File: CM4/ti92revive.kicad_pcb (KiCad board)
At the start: 2 copper layers, 205 x 116.7 mm, 219 parts, among them J1 USB_B, J2 Conn_01x02, J3 Conn_01x02, Q1 EMH3, U1 Compute_Module_4_Connectors, U3 BQ25887RGET, U4 MAX17643, U5 ATTINY85-20PU, U6 TQ2SA-L2-3V-Z-Remake

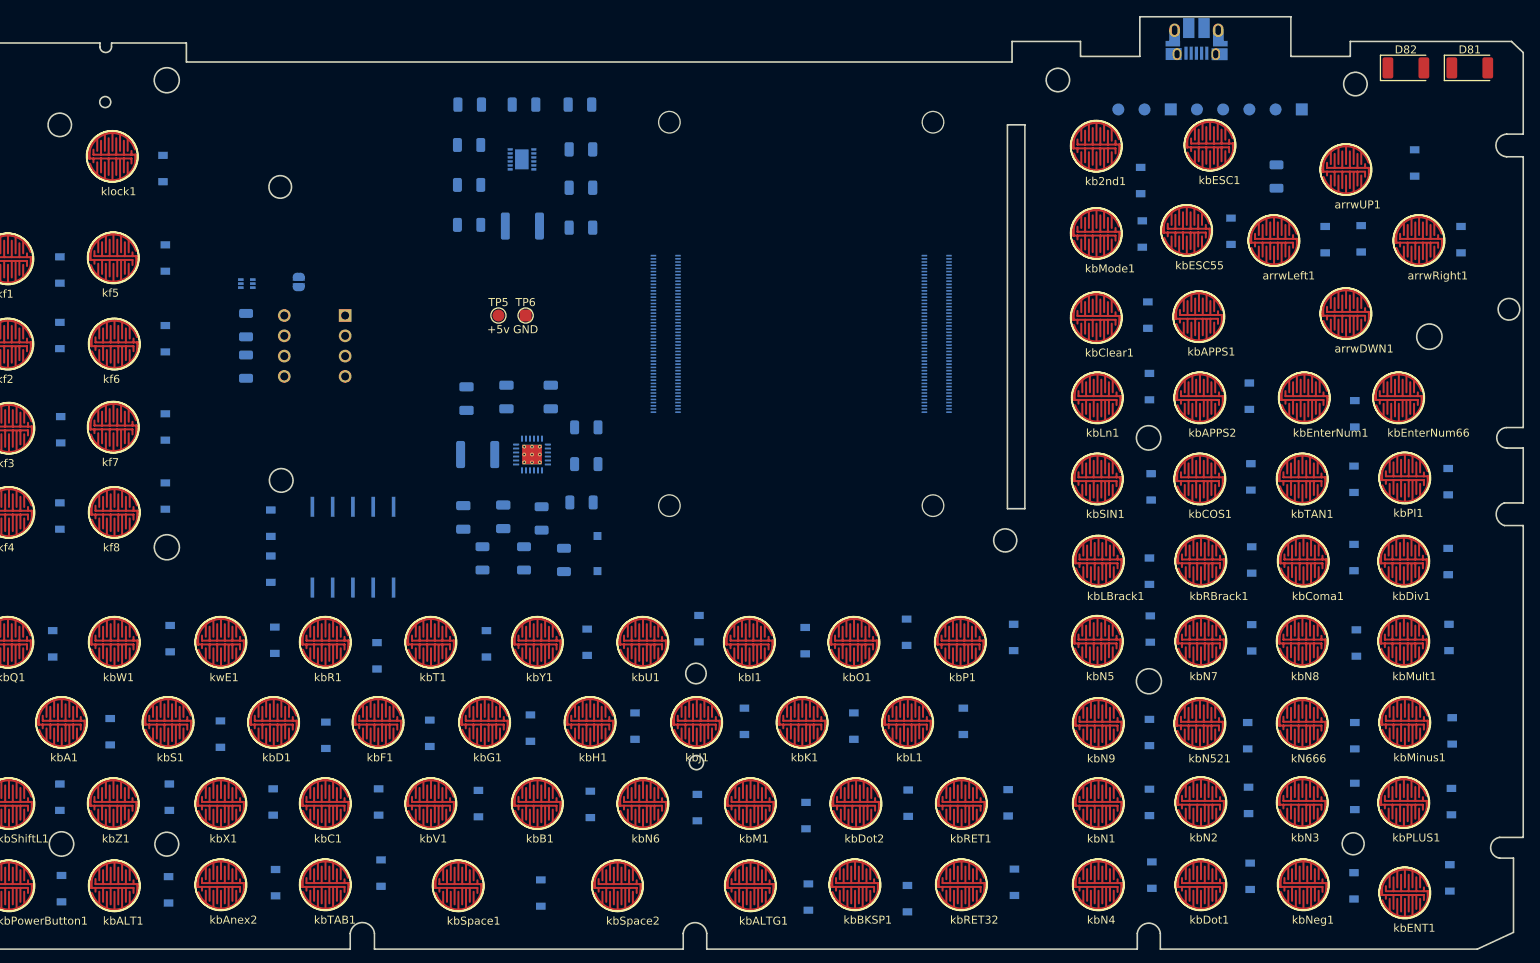
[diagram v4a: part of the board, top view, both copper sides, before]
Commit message: Removed Keyboard Matrix Diodes and Added PowerLED and ActivityLED
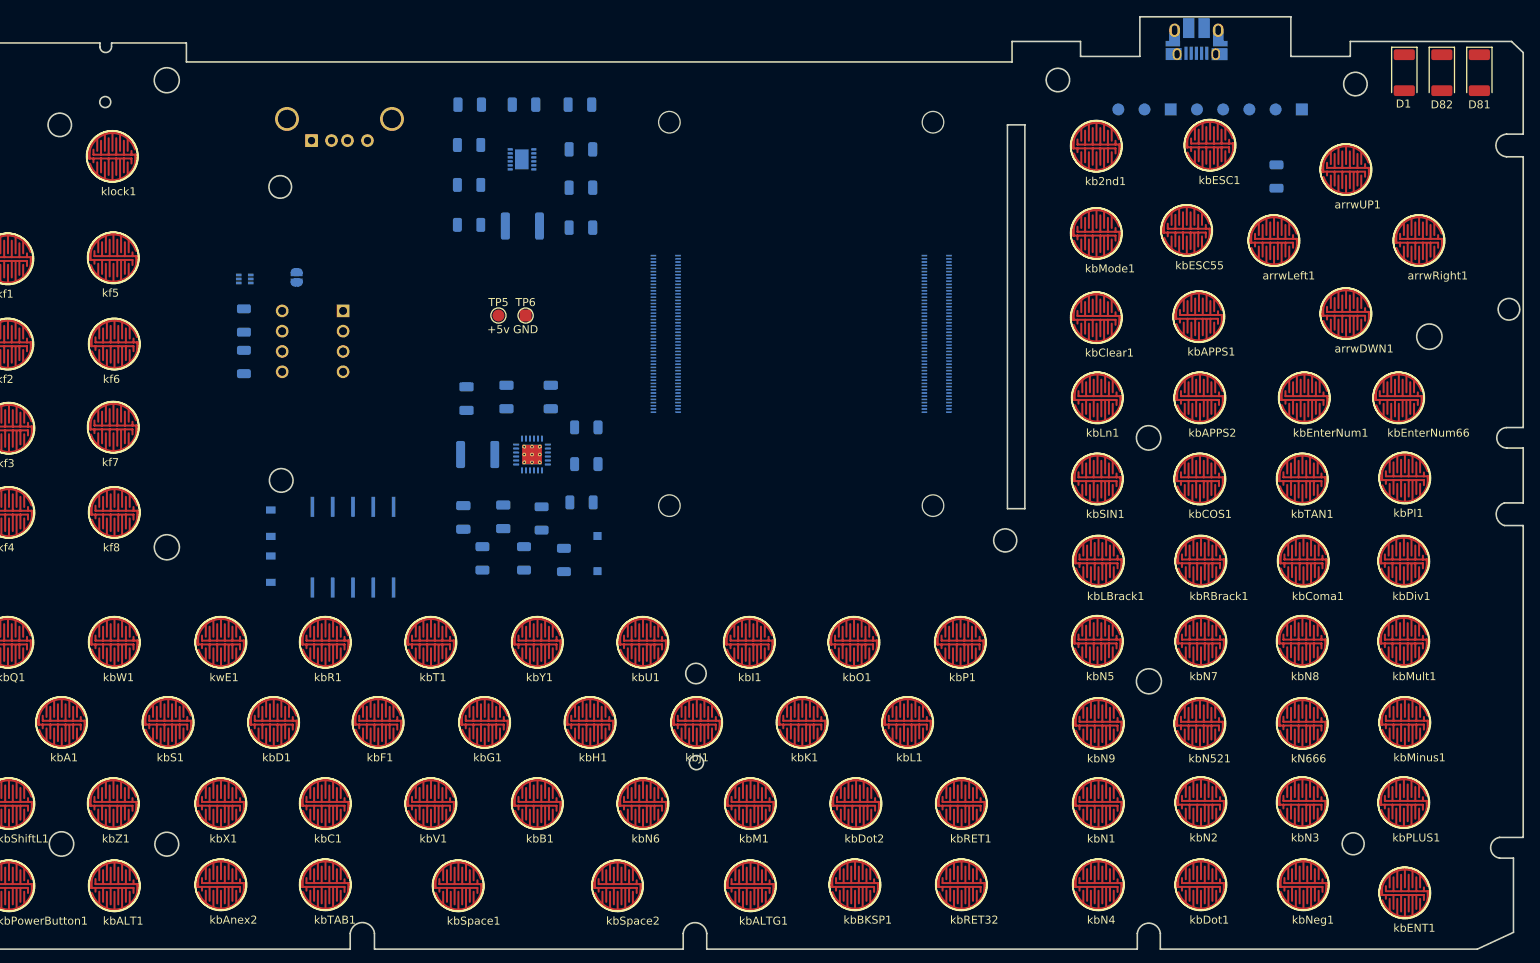
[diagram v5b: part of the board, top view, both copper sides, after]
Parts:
- removed D0, D10, D11, D12, D13, D14, D15, D16, D17, D18, D19, D2, D20, D21, D22, D23, D24, D25, D26, D27, D28, D29, D3, D30, D31, D32, D33, D34, D35, D36, D37, D38, D39, D4, D40, D41, D42, D43, D44, D45, D46, D47, D48, D49, D5, D50, D51, D52, D53, D54, D55, D56, D57, D58, D59, D6, D60, D61, D62, D63, D64, D65, D66, D67, D68, D69, D7, D70, D71, D72, D73, D74, D75, D76, D77, D78, D79, D8, D80, D9: 1N4148W, Diode_SMD:D_SOD-123
- added J4: USB_A, Connector_USB:USB_A_Stewart_SS-52100-001_Horizontal, B.Cu at (106.0, 47.9)
- D1: value 1N4148W -> Activity; footprint Diode_SMD:D_SOD-123 -> LED_SMD:LED_2010_5025Metric; moved to F.Cu
- JP1: value SolderJumper_2_Open -> PowerControllerBipass
- R12: value 330 -> 1K
- moved D1 170.1 mm to (242.8, 39.4), turned to -90 degrees
- moved D82 4.54 mm to (247.5, 39.4), turned to -90 degrees
- moved D81 1.34 mm to (252.2, 39.4), turned to -90 degrees
- moved JP1 0.64 mm to (104.1, 65.0)
- moved Q1 0.64 mm to (97.6, 65.2)
- moved R12 0.64 mm to (97.5, 70.4)
- moved R13 0.64 mm to (97.5, 75.6)
- moved U5 0.64 mm to (110.0, 69.2)
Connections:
- D1 pad 1: row0 -> +3.3
- R12 pad 1: unconnected-(R12-Pad1) -> Net-(D1-Pad2)
- R12 pad 2: Net-(R12-Pad2) -> Net-(U1-Pad21)
- U1 pad 101: unconnected-(U1-Pad101) -> Net-(U1-Pad101)
- U1 pad 103: unconnected-(U1-Pad103) -> Net-(U1-Pad103)
- U1 pad 105: unconnected-(U1-Pad105) -> Net-(U1-Pad105)
- U1 pad 21: unconnected-(U1-Pad21) -> Net-(U1-Pad21)
- U1 pad 30: unconnected-(U1-Pad30) -> piWatchDogPin
- U5 pad 3: unconnected-(U5-Pad3) -> piWatchDogPin
- arrwDWN1 pad 2: Net-(D77-Pad2) -> row4
- arrwLeft1 pad 1: col6 -> col3
- arrwLeft1 pad 2: Net-(D55-Pad2) -> row4
- arrwRight1 pad 2: Net-(D62-Pad2) -> row4
- arrwUP1 pad 2: Net-(D69-Pad2) -> row4
- kN666 pad 2: Net-(D9-Pad2) -> row0
- kb2nd1 pad 2: Net-(D14-Pad2) -> row5
- kbA1 pad 2: Net-(D11-Pad2) -> col3
- kbALT1 pad 1: col2 -> col3
- kbALT1 pad 2: Net-(D27-Pad2) -> row4
- kbALTG1 pad 1: col4 -> col3
- kbALTG1 pad 2: Net-(D41-Pad2) -> row4
- kbAPPS1 pad 1: col5 -> col3
- kbAPPS1 pad 2: Net-(D47-Pad2) -> row5
- kbAPPS2 pad 1: col5 -> col3
- kbAPPS2 pad 2: Net-(D47-Pad2) -> row5
- kbAnex2 pad 2: Net-(D80-Pad2) -> row7
- kbB1 pad 1: col5 -> col3
- kbB1 pad 2: Net-(D45-Pad2) -> col3
- kbBKSP1 pad 2: Net-(D74-Pad2) -> col3
- kbC1 pad 2: Net-(D34-Pad2) -> col3
- kbCOS1 pad 2: Net-(D70-Pad2) -> row5
- kbClear1 pad 2: Net-(D35-Pad2) -> row5
- kbComa1 pad 2: Net-(D36-Pad2) -> row6
- kbD1 pad 1: col2 -> col3
- kbD1 pad 2: Net-(D25-Pad2) -> col3
- kbDiv1 pad 1: col4 -> col3
- kbDiv1 pad 2: Net-(D43-Pad2) -> row6
- kbDot1 pad 1: col5 -> col3
- kbDot1 pad 2: Net-(D49-Pad2) -> row7
- kbDot2 pad 2: Net-(D68-Pad2) -> col3
- kbENT1 pad 2: Net-(D65-Pad2) -> row7
- kbESC1 pad 1: col1 -> col3
- kbESC1 pad 2: Net-(D21-Pad2) -> row5
- kbESC55 pad 1: col1 -> col3
- kbESC55 pad 2: Net-(D21-Pad2) -> row5
- kbEnterNum1 pad 1: col6 -> col3
- kbEnterNum1 pad 2: Net-(D56-Pad2) -> row5
- kbEnterNum66 pad 1: col6 -> col3
- kbEnterNum66 pad 2: Net-(D56-Pad2) -> row5
- kbF1 pad 2: Net-(D33-Pad2) -> col3
- kbG1 pad 1: col4 -> col3
- kbG1 pad 2: Net-(D39-Pad2) -> col3
- kbH1 pad 1: col5 -> col3
- kbH1 pad 2: Net-(D51-Pad2) -> col3
- kbI1 pad 2: Net-(D59-Pad2) -> col3
- kbJ1 pad 1: col6 -> col3
- kbJ1 pad 2: Net-(D53-Pad2) -> col3
- kbK1 pad 2: Net-(D60-Pad2) -> col3
- kbL1 pad 2: Net-(D67-Pad2) -> col3
- kbLBrack1 pad 1: col1 -> col3
- kbLBrack1 pad 2: Net-(D22-Pad2) -> row6
- kbLn1 pad 1: col4 -> col3
- kbLn1 pad 2: Net-(D42-Pad2) -> row5
- kbM1 pad 2: Net-(D61-Pad2) -> col3
- kbMinus1 pad 2: Net-(D72-Pad2) -> row7
- kbMode1 pad 1: col2 -> col3
- kbMode1 pad 2: Net-(D28-Pad2) -> row5
- kbMult1 pad 2: Net-(D71-Pad2) -> row6
- kbN1 pad 2: Net-(D16-Pad2) -> row7
- kbN2 pad 1: col1 -> col3
- kbN2 pad 2: Net-(D23-Pad2) -> row7
- kbN3 pad 1: col2 -> col3
- kbN3 pad 2: Net-(D30-Pad2) -> row7
- kbN4 pad 1: col4 -> col3
- kbN4 pad 2: Net-(D44-Pad2) -> row7
- kbN5 pad 1: col5 -> col3
- kbN5 pad 2: Net-(D48-Pad2) -> row6
- kbN521 pad 1: col5 -> col3
- kbN521 pad 2: Net-(D46-Pad2) -> row4
- kbN6 pad 1: col6 -> col3
- kbN6 pad 2: Net-(D54-Pad2) -> col3
- kbN7 pad 1: col6 -> col3
- kbN7 pad 2: Net-(D57-Pad2) -> row6
- kbN8 pad 2: Net-(D64-Pad2) -> row6
- kbN9 pad 2: Net-(D79-Pad2) -> row6
- kbNeg1 pad 1: col6 -> col3
- kbNeg1 pad 2: Net-(D58-Pad2) -> row7
- kbO1 pad 2: Net-(D66-Pad2) -> col3
- kbP1 pad 2: Net-(D73-Pad2) -> col3
- kbPI1 pad 2: Net-(D15-Pad2) -> row6
- kbPLUS1 pad 2: Net-(D37-Pad2) -> row7
- kbQ1 pad 2: Net-(D10-Pad2) -> col3
- kbR1 pad 2: Net-(D32-Pad2) -> col3
- kbRBrack1 pad 1: col2 -> col3
- kbRBrack1 pad 2: Net-(D29-Pad2) -> row6
- kbRET1 pad 2: Net-(D76-Pad2) -> col3
- kbRET32 pad 2: Net-(D75-Pad2) -> col3
- kbS1 pad 1: col1 -> col3
- kbS1 pad 2: Net-(D18-Pad2) -> col3
- kbSIN1 pad 2: Net-(D63-Pad2) -> row5
- kbShiftL1 pad 1: col1 -> col3
- kbShiftL1 pad 2: Net-(D20-Pad2) -> row4
- kbSpace1 pad 2: Net-(D31-Pad2) -> row4
- kbSpace2 pad 2: Net-(D31-Pad2) -> row4
- kbT1 pad 1: col4 -> col3
- kbT1 pad 2: Net-(D38-Pad2) -> col3
- kbTAB1 pad 2: Net-(D12-Pad2) -> col3
- kbTAN1 pad 2: Net-(D78-Pad2) -> row5
- kbU1 pad 1: col6 -> col3
- kbU1 pad 2: Net-(D52-Pad2) -> col3
- kbV1 pad 1: col4 -> col3
- kbV1 pad 2: Net-(D40-Pad2) -> col3
- kbW1 pad 1: col1 -> col3
- kbW1 pad 2: Net-(D17-Pad2) -> col3
- kbX1 pad 1: col2 -> col3
- kbX1 pad 2: Net-(D26-Pad2) -> col3
- kbY1 pad 1: col5 -> col3
- kbY1 pad 2: Net-(D50-Pad2) -> col3
- kbZ1 pad 1: col1 -> col3
- kbZ1 pad 2: Net-(D19-Pad2) -> col3
- kf1 pad 1: col1 -> col3
- kf1 pad 2: Net-(D1-Pad2) -> row0
- kf2 pad 1: col2 -> col3
- kf2 pad 2: Net-(D3-Pad2) -> row0
- kf3 pad 2: Net-(D2-Pad2) -> row0
- kf4 pad 1: col4 -> col3
- kf4 pad 2: Net-(D4-Pad2) -> row0
- kf5 pad 1: col5 -> col3
- kf5 pad 2: Net-(D5-Pad2) -> row0
- kf6 pad 1: col6 -> col3
- kf6 pad 2: Net-(D6-Pad2) -> row0
- kf7 pad 2: Net-(D7-Pad2) -> row0
- kf8 pad 2: Net-(D8-Pad2) -> row0
- klock1 pad 2: Net-(D0-Pad2) -> row0
- kwE1 pad 1: col2 -> col3
- kwE1 pad 2: Net-(D24-Pad2) -> col3

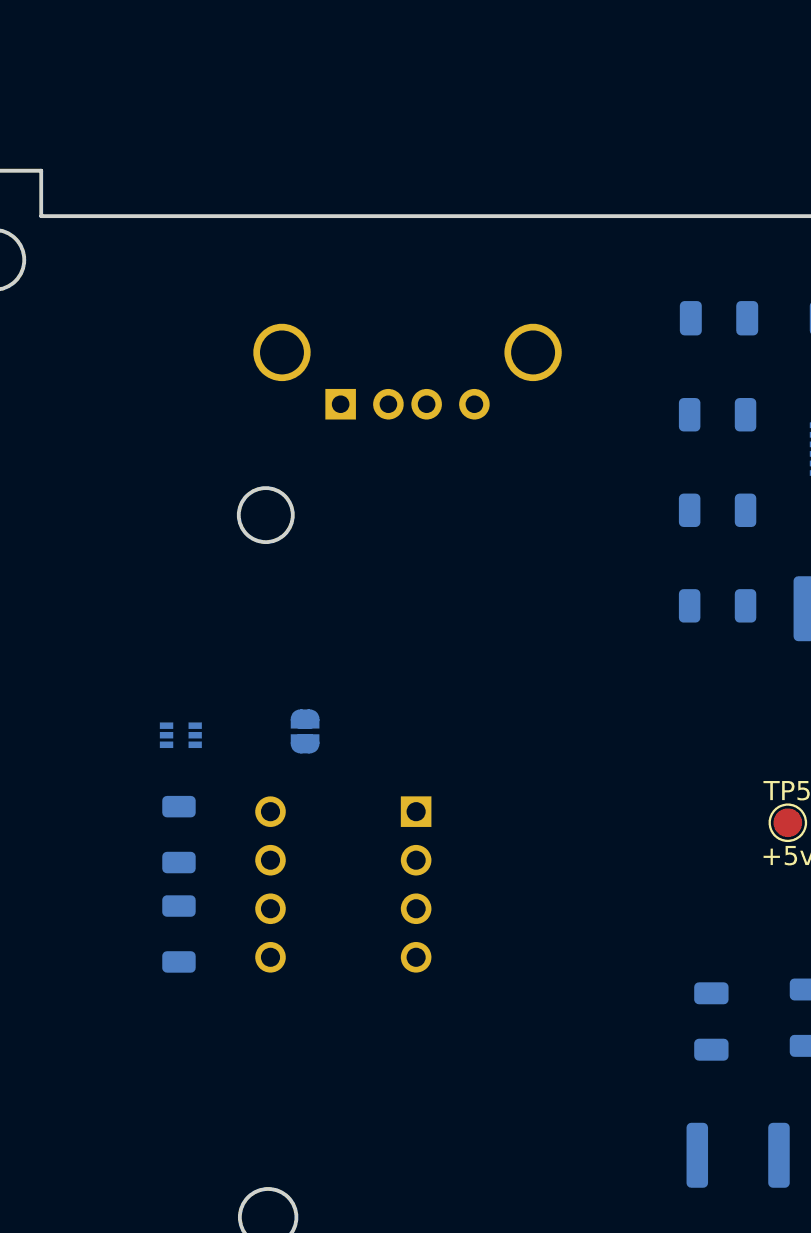
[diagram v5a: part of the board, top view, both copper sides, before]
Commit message: Added high current 3.3v supply
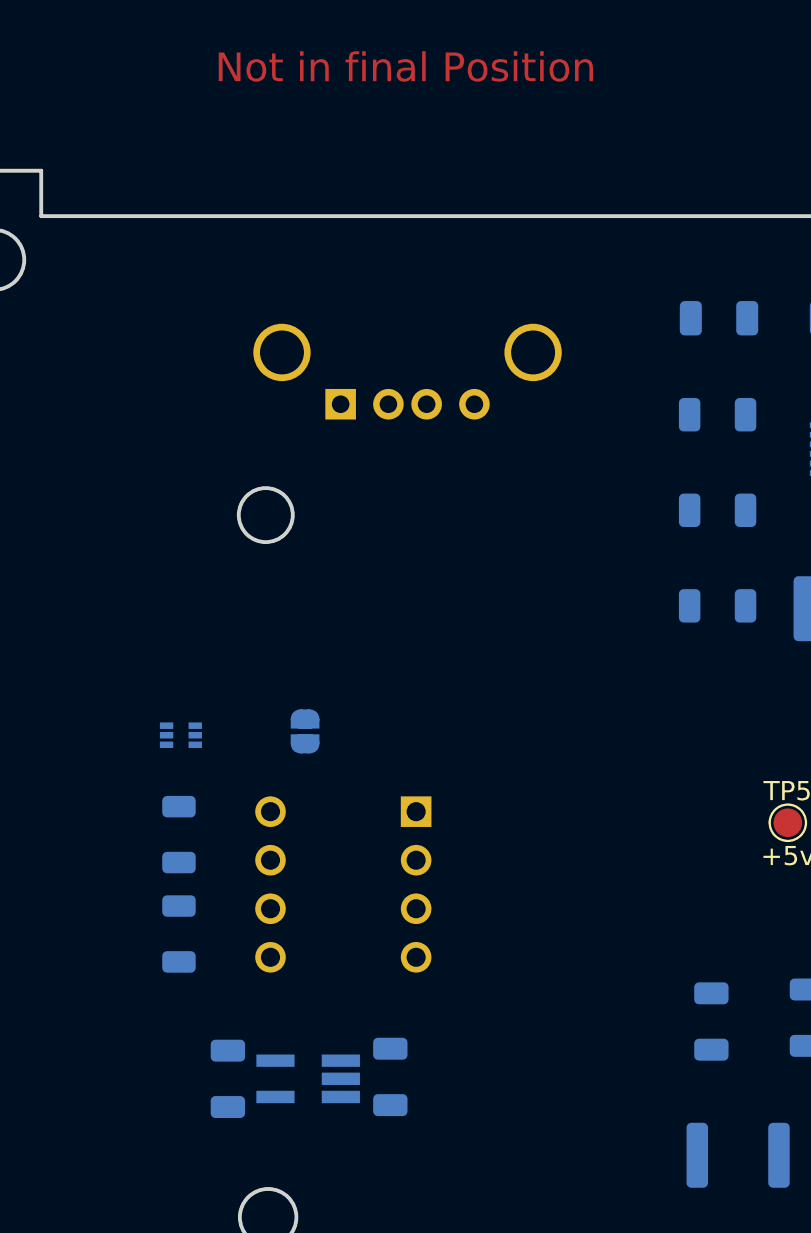
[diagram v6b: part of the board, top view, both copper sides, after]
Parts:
- added C12: 10 uF, Capacitor_SMD:C_1206_3216Metric, B.Cu at (108.6, 83.1)
- added C13: 10 uF, Capacitor_SMD:C_1206_3216Metric, B.Cu at (100.1, 83.2)
- added U2: NCP114ASN330T1G, Package_TO_SOT_SMD:TSOT-23-5_HandSoldering, B.Cu at (104.3, 83.2)
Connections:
- net col3 renamed col1
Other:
- board text added: "Not in final Position"

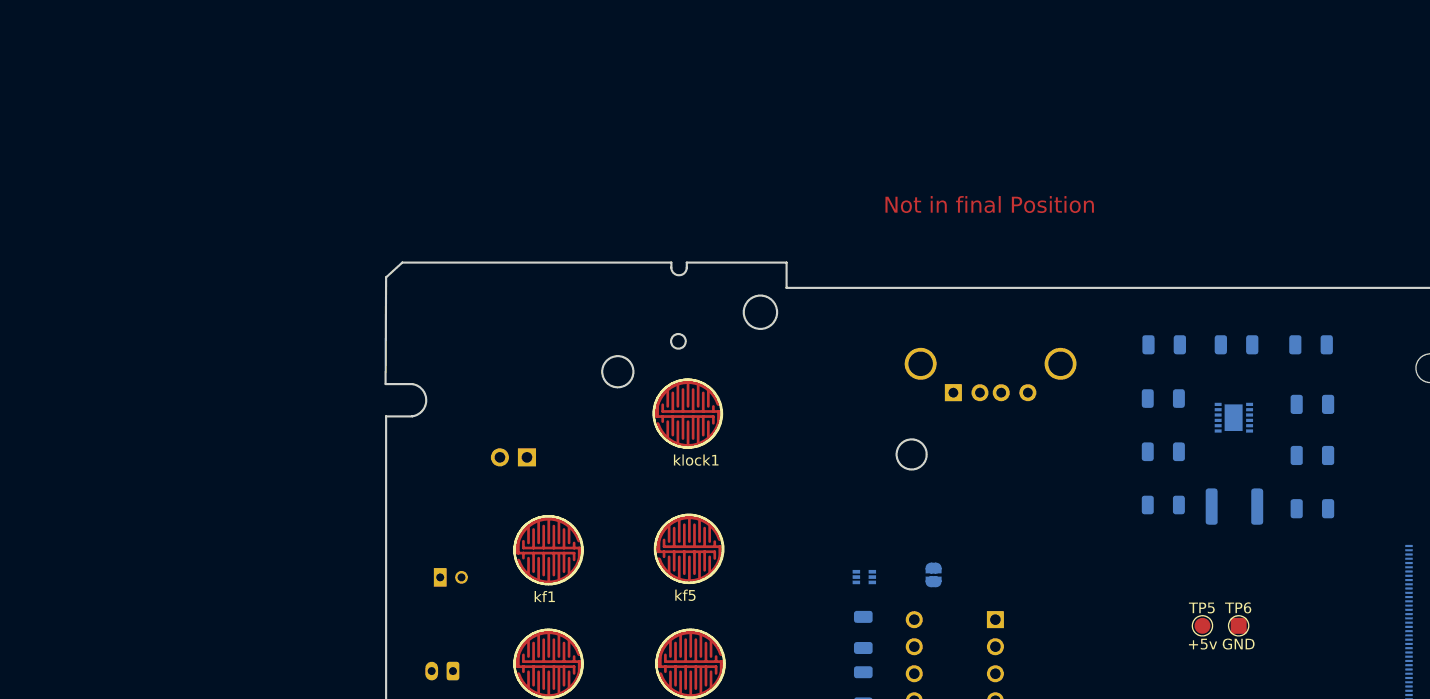
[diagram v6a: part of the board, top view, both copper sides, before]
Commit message: Added USB Hub Contoler and usb port internal and external
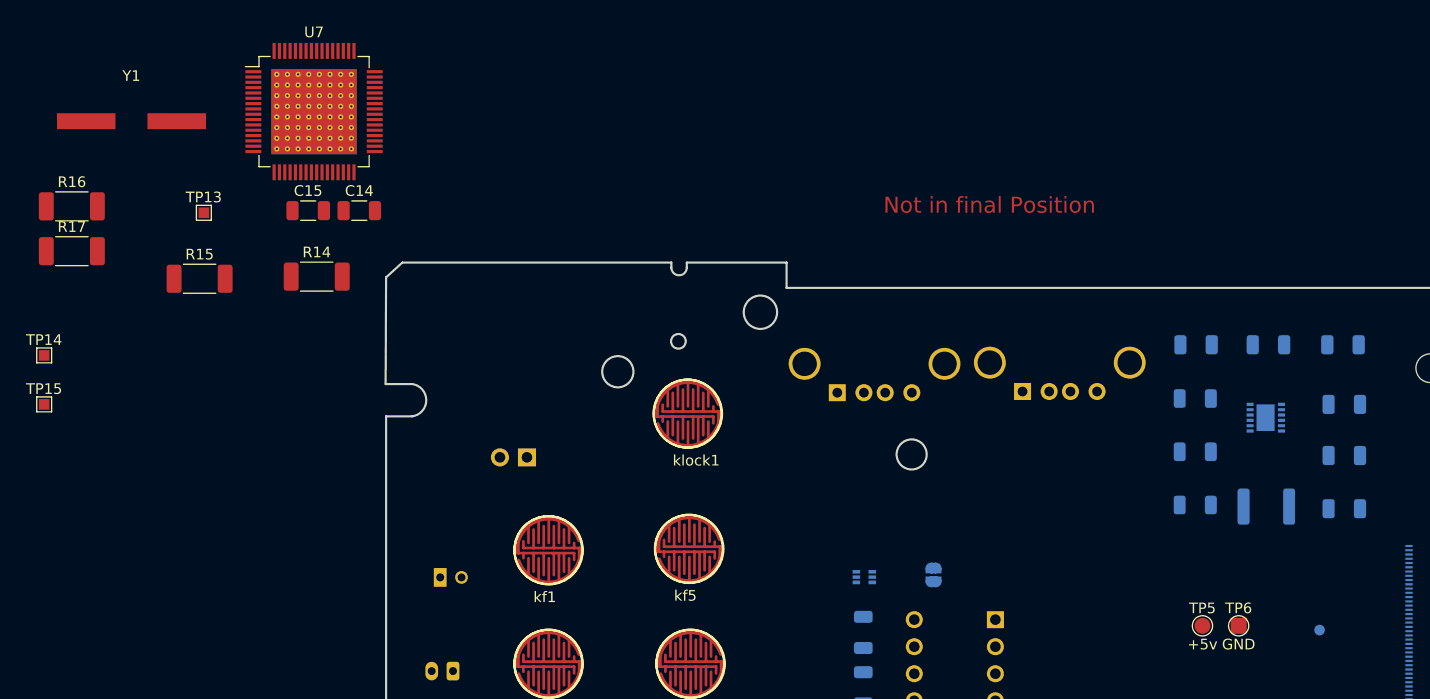
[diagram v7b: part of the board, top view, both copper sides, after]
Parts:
- added C14: CL1, Capacitor_SMD:C_1206_3216Metric, F.Cu at (50.2, 30.8)
- added C15: CL2, Capacitor_SMD:C_1206_3216Metric, F.Cu at (45.4, 30.8)
- added J5: USB_A, Connector_USB:USB_A_Stewart_SS-52100-001_Horizontal, B.Cu at (112.5, 47.8)
- added R14: 10 M, Resistor_SMD:R_2010_5025Metric_Pad1.40x2.65mm_HandSolder, F.Cu at (46.2, 37.0)
- added R15: 9.53K +-1%, Resistor_SMD:R_2010_5025Metric_Pad1.40x2.65mm_HandSolder, F.Cu at (35.2, 37.2)
- added R16: 90.9k +-1%, Resistor_SMD:R_2010_5025Metric_Pad1.40x2.65mm_HandSolder, F.Cu at (23.2, 30.4)
- added R17: 10k +-1%, Resistor_SMD:R_2010_5025Metric_Pad1.40x2.65mm_HandSolder, F.Cu at (23.2, 34.6)
- added TP12: USB_OTG_ID_TP, TestPoint:TestPoint_Pad_D1.0mm, B.Cu at (140.4, 70.2)
- added TP13: GRSTz, TestPoint:TestPoint_Pad_1.0x1.0mm, F.Cu at (35.6, 31.0)
- added TP14: USB_DP_DN4, TestPoint:TestPoint_Pad_1.0x1.0mm, F.Cu at (20.6, 44.4)
- added TP15: USB_DM_DN4, TestPoint:TestPoint_Pad_1.0x1.0mm, F.Cu at (20.6, 49.0)
- added U7: TUSB4041I, Package_QFP:HTQFP-64-1EP_10x10mm_P0.5mm_EP8x8mm_Mask4.4x4.4mm_ThermalVias, F.Cu at (46.0, 21.5)
- added Y1: 24 MHz, teensy:HCM49_E, F.Cu at (28.8, 22.4)
- moved J4 10.9 mm to (95.1, 47.9)
- moved C11 3.00 mm to (128.8, 43.4)
- moved C10 3.00 mm to (135.6, 43.4)
- moved C6 3.00 mm to (142.7, 53.8)
- moved C7 3.00 mm to (142.7, 49.0)
- moved C8 3.00 mm to (142.7, 58.8)
- moved C9 3.00 mm to (142.6, 43.4)
- moved L2 3.00 mm to (135.4, 58.6)
- moved R10 3.00 mm to (128.7, 58.5)
- moved R11 3.00 mm to (128.7, 53.5)
- moved R9 3.00 mm to (128.7, 48.5)
- moved U4 3.00 mm to (135.3, 50.2)
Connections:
- J4 pad 2: Net-(J4-Pad2) -> Net-(U7-Pad34)
- U1 pad 103: Net-(J4-Pad2) -> USB_HOST_N
- U1 pad 105: Net-(J4-Pad3) -> USB_HOST_P
- U2 pad 3: +3.3 -> +1.8
